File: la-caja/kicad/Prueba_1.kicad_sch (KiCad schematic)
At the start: 18 parts

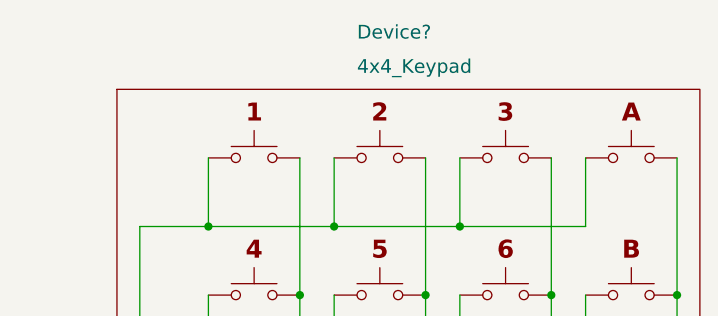
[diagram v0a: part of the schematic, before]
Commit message: Esquematico actualizado, nuevo símbolo para numpad
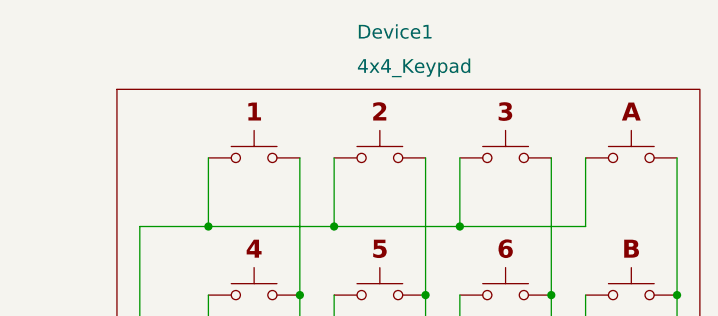
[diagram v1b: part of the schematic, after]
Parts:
- gave numbers to parts that had none: 17
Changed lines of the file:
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@@
   (symbol (lib_id "Switch:SW_Push") (at 151.13 36.83 0) (unit 1)
     (in_bom yes) (on_board yes) (fields_autoplaced)
-    (property "Reference" "SW?" (id 0) (at 151.13 29.21 0)
+    (property "Reference" "SW1" (id 0) (at 151.13 29.21 0)
       (effects (font (size 1.27 1.27)) hide)
     )
@@
   (symbol (lib_id "Switch:SW_Push") (at 193.04 67.31 0) (unit 1)
     (in_bom yes) (on_board yes) (fields_autoplaced)
-    (property "Reference" "SW?" (id 0) (at 193.04 59.69 0)
+    (property "Reference" "SW15" (id 0) (at 193.04 59.69 0)
       (effects (font (size 1.27 1.27)) hide)
     )
@@
   (symbol (lib_id "Switch:SW_Push") (at 151.13 52.07 0) (unit 1)
     (in_bom yes) (on_board yes) (fields_autoplaced)
-    (property "Reference" "SW?" (id 0) (at 151.13 44.45 0)
+    (property "Reference" "SW2" (id 0) (at 151.13 44.45 0)
       (effects (font (size 1.27 1.27)) hide)
     )
@@
   (symbol (lib_id "Switch:SW_Push") (at 165.1 36.83 0) (unit 1)
     (in_bom yes) (on_board yes) (fields_autoplaced)
-    (property "Reference" "SW?" (id 0) (at 165.1 29.21 0)
+    (property "Reference" "SW5" (id 0) (at 165.1 29.21 0)
       (effects (font (size 1.27 1.27)) hide)
     )
@@
   (symbol (lib_id "Switch:SW_Push") (at 151.13 67.31 0) (unit 1)
     (in_bom yes) (on_board yes) (fields_autoplaced)
-    (property "Reference" "SW?" (id 0) (at 151.13 59.69 0)
+    (property "Reference" "SW3" (id 0) (at 151.13 59.69 0)
       (effects (font (size 1.27 1.27)) hide)
     )
@@
   (symbol (lib_id "Switch:SW_Push") (at 193.04 36.83 0) (unit 1)
     (in_bom yes) (on_board yes) (fields_autoplaced)
-    (property "Reference" "SW?" (id 0) (at 193.04 29.21 0)
+    (property "Reference" "SW13" (id 0) (at 193.04 29.21 0)
       (effects (font (size 1.27 1.27)) hide)
     )
@@
   (symbol (lib_id "Switch:SW_Push") (at 165.1 67.31 0) (unit 1)
     (in_bom yes) (on_board yes) (fields_autoplaced)
-    (property "Reference" "SW?" (id 0) (at 165.1 59.69 0)
+    (property "Reference" "SW7" (id 0) (at 165.1 59.69 0)
       (effects (font (size 1.27 1.27)) hide)
     )
@@
   (symbol (lib_id "Switch:SW_Push") (at 165.1 52.07 0) (unit 1)
     (in_bom yes) (on_board yes) (fields_autoplaced)
-    (property "Reference" "SW?" (id 0) (at 165.1 44.45 0)
+    (property "Reference" "SW6" (id 0) (at 165.1 44.45 0)
       (effects (font (size 1.27 1.27)) hide)
     )
@@
   (symbol (lib_id "Switch:SW_Push") (at 179.07 52.07 0) (unit 1)
     (in_bom yes) (on_board yes) (fields_autoplaced)
-    (property "Reference" "SW?" (id 0) (at 179.07 44.45 0)
+    (property "Reference" "SW10" (id 0) (at 179.07 44.45 0)
       (effects (font (size 1.27 1.27)) hide)
     )
@@
   (symbol (lib_id "OwnKeyPAD:4x4_Keypad") (at 167.64 67.31 0) (unit 1)
     (in_bom yes) (on_board yes)
-    (property "Reference" "Device?" (id 0) (at 162.56 22.86 0)
+    (property "Reference" "Device1" (id 0) (at 162.56 22.86 0)
       (effects (font (size 1.524 1.524)) (justify left))
     )
@@
   (symbol (lib_id "Switch:SW_Push") (at 179.07 67.31 0) (unit 1)
     (in_bom yes) (on_board yes) (fields_autoplaced)
-    (property "Reference" "SW?" (id 0) (at 179.07 59.69 0)
+    (property "Reference" "SW11" (id 0) (at 179.07 59.69 0)
       (effects (font (size 1.27 1.27)) hide)
     )
@@
   (symbol (lib_id "Switch:SW_Push") (at 193.04 52.07 0) (unit 1)
     (in_bom yes) (on_board yes) (fields_autoplaced)
-    (property "Reference" "SW?" (id 0) (at 193.04 44.45 0)
+    (property "Reference" "SW14" (id 0) (at 193.04 44.45 0)
       (effects (font (size 1.27 1.27)) hide)
     )
@@
   (symbol (lib_id "Switch:SW_Push") (at 151.13 82.55 0) (unit 1)
     (in_bom yes) (on_board yes) (fields_autoplaced)
-    (property "Reference" "SW?" (id 0) (at 151.13 74.93 0)
+    (property "Reference" "SW4" (id 0) (at 151.13 74.93 0)
       (effects (font (size 1.27 1.27)) hide)
     )
@@
   (symbol (lib_id "Switch:SW_Push") (at 193.04 82.55 0) (unit 1)
     (in_bom yes) (on_board yes) (fields_autoplaced)
-    (property "Reference" "SW?" (id 0) (at 193.04 74.93 0)
+    (property "Reference" "SW16" (id 0) (at 193.04 74.93 0)
       (effects (font (size 1.27 1.27)) hide)
     )
@@
   (symbol (lib_id "Switch:SW_Push") (at 179.07 36.83 0) (unit 1)
     (in_bom yes) (on_board yes) (fields_autoplaced)
-    (property "Reference" "SW?" (id 0) (at 179.07 29.21 0)
+    (property "Reference" "SW9" (id 0) (at 179.07 29.21 0)
       (effects (font (size 1.27 1.27)) hide)
     )
@@
   (symbol (lib_id "Switch:SW_Push") (at 165.1 82.55 0) (unit 1)
     (in_bom yes) (on_board yes) (fields_autoplaced)
-    (property "Reference" "SW?" (id 0) (at 165.1 74.93 0)
+    (property "Reference" "SW8" (id 0) (at 165.1 74.93 0)
       (effects (font (size 1.27 1.27)) hide)
     )
@@
   (symbol (lib_id "Switch:SW_Push") (at 179.07 82.55 0) (unit 1)
     (in_bom yes) (on_board yes) (fields_autoplaced)
-    (property "Reference" "SW?" (id 0) (at 179.07 74.93 0)
-      (effects (font (size 1.27 1.27)) hide)
-    )
+    (property "Reference" "SW12" (id 0) (at 179.07 74.93 0)
+      (effects (font (size 1.27 1.27)) hide)
+    )
